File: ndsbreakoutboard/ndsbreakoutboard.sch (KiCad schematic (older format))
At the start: 2 parts, among them J1 Conn_01x17_Female, U1 ndsPADS

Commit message: Create footprint for the pad component (bottom of the cart). Basic PCB layout
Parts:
- J1: footprint (none) -> Connector_PinHeader_2.54mm:PinHeader_1x17_P2.54mm_Vertical
- U1: footprint (none) -> Connector:nds_contact_pads
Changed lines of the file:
@@
 F 0 "J1" V 2415 1980 50  0000 C CNN
 F 1 "Conn_01x17_Female" V 2324 1980 50  0000 C CNN
-F 2 "" H 2250 2000 50  0001 C CNN
+F 2 "Connector_PinHeader_2.54mm:PinHeader_1x17_P2.54mm_Vertical" H 2250 2000 50  0001 C CNN
 F 3 "~" H 2250 2000 50  0001 C CNN
 	1    2250 2000
@@
 F 0 "U1" H 2978 3942 50  0000 L CNN
 F 1 "ndsPADS" H 2978 3851 50  0000 L CNN
-F 2 "" H 2450 3400 50  0001 C CNN
+F 2 "Connector:nds_contact_pads" H 2450 3400 50  0001 C CNN
 F 3 "" H 2450 3400 50  0001 C CNN
 	1    2450 3400

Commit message: Commit before rebuilding netlist with pin headers
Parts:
- removed J1: Conn_01x17_Female, Connector_PinHeader_2.54mm:PinHeader_1x17_P2.54mm_Vertical, symbol Connector:Conn_01x17_Female
- added J1: Conn_01x01_Female, Connector_PinHeader_1.00mm:PinHeader_1x01_P1.00mm_Horizontal, symbol Connector:Conn_01x01_Female
- added J2: Conn_01x07_Female, Connector_PinHeader_1.00mm:PinHeader_1x07_P1.00mm_Horizontal, symbol Connector:Conn_01x07_Female
- added J3: Conn_01x08_Female, Connector_PinHeader_1.00mm:PinHeader_1x08_P1.00mm_Horizontal, symbol Connector:Conn_01x08_Female
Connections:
- net at U1.1 (GND): now also U1.17 (GND), J1.1 (Pin_1)
- net at U1.10 (D1): now also J3.7 (Pin_7)
- net at U1.11 (D2): now also J3.6 (Pin_6)
- net at U1.12 (D3): now also J3.5 (Pin_5)
- net at U1.13 (D5): now also J3.4 (Pin_4)
- net at U1.14 (D4): now also J3.3 (Pin_3)
- net at U1.15 (D6): now also J3.2 (Pin_2)
- net at U1.16 (D7): now also J3.1 (Pin_1)
- net at U1.2 (CLK): now also J2.7 (Pin_7)
- net at U1.3 (UNUSED): now also J2.6 (Pin_6)
- net at U1.4 (CS1_ROM): now also J2.5 (Pin_5)
- net at U1.5 (RESET): now also J2.4 (Pin_4)
- net at U1.6 (CS2_EEPROM): now also J2.3 (Pin_3)
- net at U1.7 (IRQ): now also J2.2 (Pin_2)
- net at U1.8 (3.3V): now also J2.1 (Pin_1)
- net at U1.9 (D0): now also J3.8 (Pin_8)
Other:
- moved on the sheet: U1
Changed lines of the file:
@@
 $EndDescr
-$Comp
-L Connector:Conn_01x17_Female J1
-U 1 1 5FF23434
-P 2250 2000
-F 0 "J1" V 2415 1980 50  0000 C CNN
-F 1 "Conn_01x17_Female" V 2324 1980 50  0000 C CNN
-F 2 "Connector_PinHeader_2.54mm:PinHeader_1x17_P2.54mm_Vertical" H 2250 2000 50  0001 C CNN
-F 3 "~" H 2250 2000 50  0001 C CNN
-	1    2250 2000
-	0    -1   -1   0
-$EndComp
 $Comp
 L Connector:ndsPADS U1
 U 1 1 5FF2F120
-P 2450 3400
-F 0 "U1" H 2978 3942 50  0000 L CNN
-F 1 "ndsPADS" H 2978 3851 50  0000 L CNN
-F 2 "Connector:nds_contact_pads" H 2450 3400 50  0001 C CNN
-F 3 "" H 2450 3400 50  0001 C CNN
-	1    2450 3400
+P 3050 2550
+F 0 "U1" H 3578 3092 50  0000 L CNN
+F 1 "ndsPADS" H 3578 3001 50  0000 L CNN
+F 2 "Connector:nds_contact_pads" H 3050 2550 50  0001 C CNN
+F 3 "" H 3050 2550 50  0001 C CNN
+	1    3050 2550
 	1    0    0    -1
 $EndComp
+$Comp
+L Connector:Conn_01x08_Female J3
+U 1 1 5FF67247
+P 3250 2450
+F 0 "J3" V 3323 2380 50  0000 C CNN
+F 1 "Conn_01x08_Female" V 3414 2380 50  0000 C CNN
+F 2 "Connector_PinHeader_1.00mm:PinHeader_1x08_P1.00mm_Horizontal" H 3250 2450 50  0001 C CNN
+F 3 "~" H 3250 2450 50  0001 C CNN
+	1    3250 2450
+	0    1    1    0
+$EndComp
+$Comp
+L Connector:Conn_01x07_Female J2
+U 1 1 5FF6AEC4
+P 2450 2450
+F 0 "J2" V 2523 2430 50  0000 C CNN
+F 1 "Conn_01x07_Female" V 2614 2430 50  0000 C CNN
+F 2 "Connector_PinHeader_1.00mm:PinHeader_1x07_P1.00mm_Horizontal" H 2450 2450 50  0001 C CNN
+F 3 "~" H 2450 2450 50  0001 C CNN
+	1    2450 2450
+	0    1    1    0
+$EndComp
+$Comp
+L Connector:Conn_01x01_Female J1
+U 1 1 5FF6C91E
+P 2050 3150
+F 0 "J1" V 1896 3198 50  0000 L CNN
+F 1 "Conn_01x01_Female" V 1987 3198 50  0000 L CNN
+F 2 "Connector_PinHeader_1.00mm:PinHeader_1x01_P1.00mm_Horizontal" H 2050 3150 50  0001 C CNN
+F 3 "~" H 2050 3150 50  0001 C CNN
+	1    2050 3150
+	0    1    1    0
+$EndComp
 Wire Wire Line
-	1450 2200 1450 3100
+	2050 2950 3650 2950
 Wire Wire Line
-	1550 2200 1550 3100
+	3650 2950 3650 2250
 Wire Wire Line
-	1650 2200 1650 3100
-Wire Wire Line
-	1750 2200 1750 3100
-Wire Wire Line
-	1850 2200 1850 3100
-Wire Wire Line
-	1950 2200 1950 3100
-Wire Wire Line
-	2050 2200 2050 3100
-Wire Wire Line
-	2150 2200 2150 3100
-Wire Wire Line
-	2250 2200 2250 3100
-Wire Wire Line
-	2350 2200 2350 3100
-Wire Wire Line
-	2450 2200 2450 3100
-Wire Wire Line
-	2550 2200 2550 3100
-Wire Wire Line
-	2650 2200 2650 3100
-Wire Wire Line
-	2750 3100 2750 2200
-Wire Wire Line
-	2850 2200 2850 3100
-Wire Wire Line
-	2950 2200 2950 3100
-Wire Wire Line
-	3050 2200 3050 3100
+	2050 2950 2050 2250
+Connection ~ 2050 2950
 $EndSCHEMATC

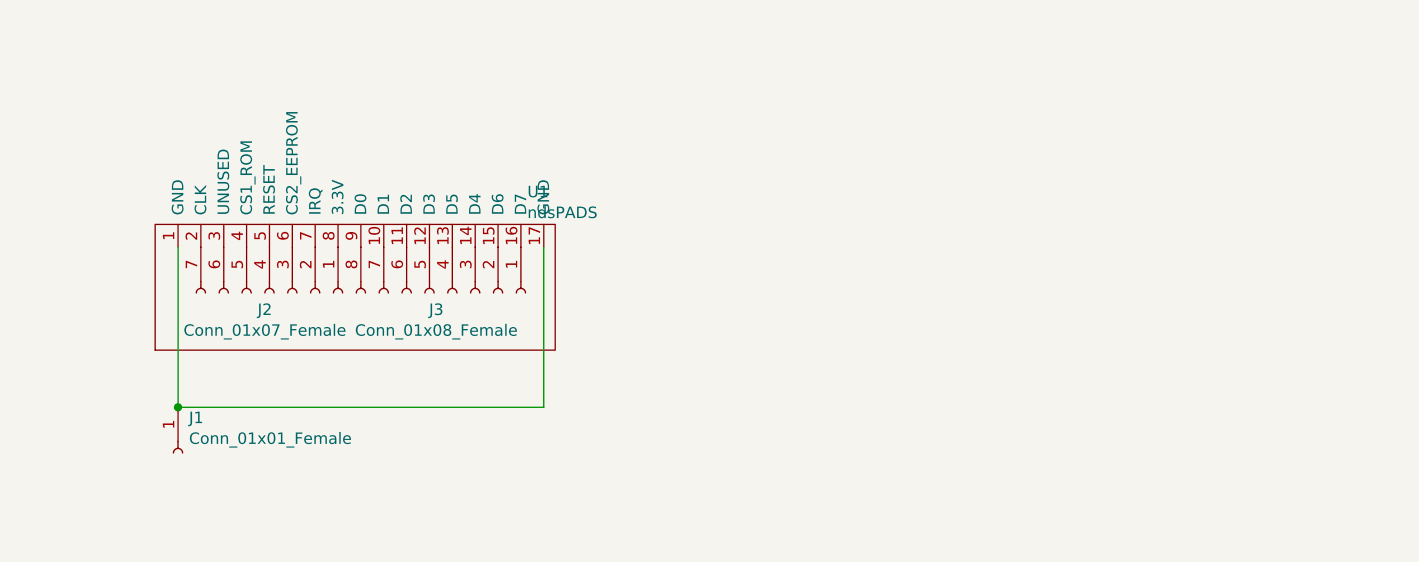
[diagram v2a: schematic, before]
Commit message: Final iteration finished
- correct eschematics
- pcb design finished
- pcb improvements
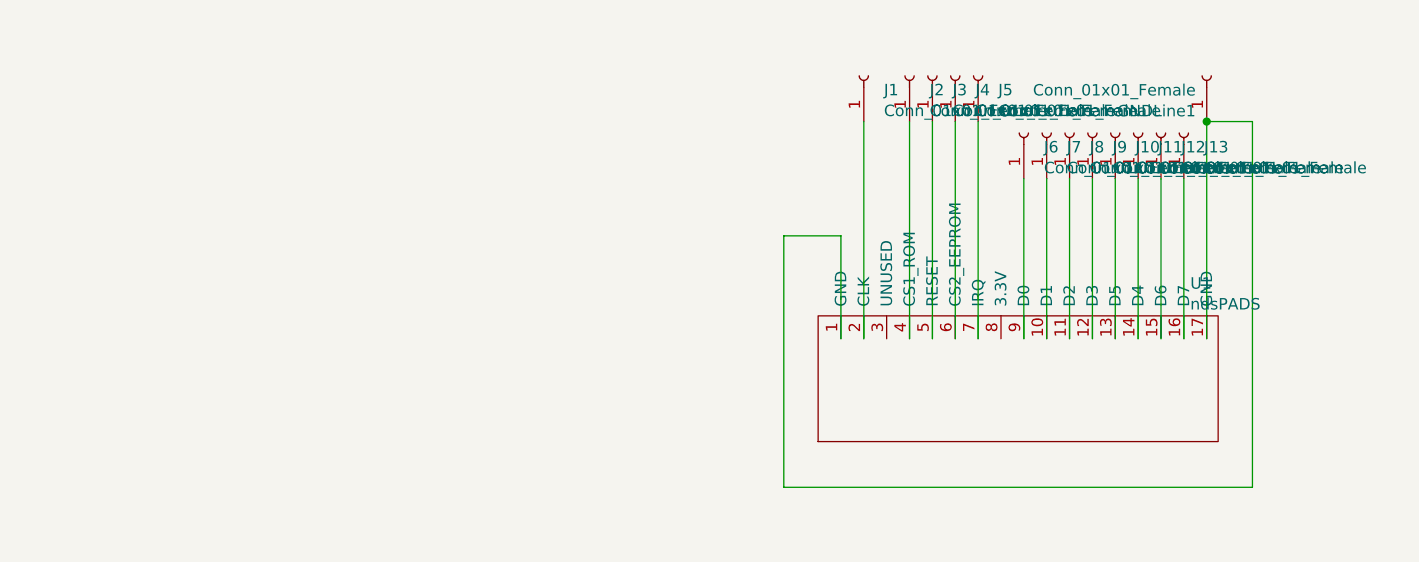
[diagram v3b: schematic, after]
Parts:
- removed J2: Conn_01x07_Female, Connector_PinHeader_1.00mm:PinHeader_1x07_P1.00mm_Horizontal, symbol Connector:Conn_01x07_Female
- removed J3: Conn_01x08_Female, Connector_PinHeader_1.00mm:PinHeader_1x08_P1.00mm_Horizontal, symbol Connector:Conn_01x08_Female
- added J1, J10, J11, J12, J13, J2, J3, J4, J5, J6, J7, J8, J9: Conn_01x01_Female, Connector_PinHeader_1.00mm:PinHeader_1x01_P1.00mm_Horizontal, symbol Connector:Conn_01x01_Female
- renumbered J1 to GNDLine1
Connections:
- net at U1.10 (D1): now also J7.1 (Pin_1)
- net at U1.11 (D2): now also J8.1 (Pin_1)
- net at U1.12 (D3): now also J9.1 (Pin_1)
- net at U1.13 (D5): now also J10.1 (Pin_1)
- net at U1.14 (D4): now also J11.1 (Pin_1)
- net at U1.15 (D6): now also J12.1 (Pin_1)
- net at U1.16 (D7): now also J13.1 (Pin_1)
- net at U1.2 (CLK): now also J1.1 (Pin_1)
- net at U1.4 (CS1_ROM): now also J2.1 (Pin_1)
- net at U1.5 (RESET): now also J3.1 (Pin_1)
- net at U1.6 (CS2_EEPROM): now also J4.1 (Pin_1)
- net at U1.7 (IRQ): now also J5.1 (Pin_1)
- net at U1.9 (D0): now also J6.1 (Pin_1)
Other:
- moved on the sheet: GNDLine1, U1
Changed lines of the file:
@@
 $EndDescr
+$Comp
+L Connector:Conn_01x01_Female GNDLine1
+U 1 1 5FF6C91E
+P 6550 1500
+F 0 "GNDLine1" V 6396 1548 50  0000 L CNN
+F 1 "Conn_01x01_Female" V 6487 1548 50  0000 L CNN
+F 2 "Connector_PinHeader_1.00mm:PinHeader_1x01_P1.00mm_Horizontal" H 6550 1500 50  0001 C CNN
+F 3 "~" H 6550 1500 50  0001 C CNN
+	1    6550 1500
+	0    -1   -1   0
+$EndComp
 $Comp
 L Connector:ndsPADS U1
 U 1 1 5FF2F120
-P 3050 2550
-F 0 "U1" H 3578 3092 50  0000 L CNN
-F 1 "ndsPADS" H 3578 3001 50  0000 L CNN
-F 2 "Connector:nds_contact_pads" H 3050 2550 50  0001 C CNN
-F 3 "" H 3050 2550 50  0001 C CNN
-	1    3050 2550
+P 5950 2950
+F 0 "U1" H 6478 3492 50  0000 L CNN
+F 1 "ndsPADS" H 6478 3401 50  0000 L CNN
+F 2 "Connector:nds_contact_pads" H 5950 2950 50  0001 C CNN
+F 3 "" H 5950 2950 50  0001 C CNN
+	1    5950 2950
 	1    0    0    -1
 $EndComp
-$Comp
-L Connector:Conn_01x08_Female J3
-U 1 1 5FF67247
-P 3250 2450
-F 0 "J3" V 3323 2380 50  0000 C CNN
-F 1 "Conn_01x08_Female" V 3414 2380 50  0000 C CNN
-F 2 "Connector_PinHeader_1.00mm:PinHeader_1x08_P1.00mm_Horizontal" H 3250 2450 50  0001 C CNN
-F 3 "~" H 3250 2450 50  0001 C CNN
-	1    3250 2450
-	0    1    1    0
-$EndComp
-$Comp
-L Connector:Conn_01x07_Female J2
-U 1 1 5FF6AEC4
-P 2450 2450
-F 0 "J2" V 2523 2430 50  0000 C CNN
-F 1 "Conn_01x07_Female" V 2614 2430 50  0000 C CNN
-F 2 "Connector_PinHeader_1.00mm:PinHeader_1x07_P1.00mm_Horizontal" H 2450 2450 50  0001 C CNN
-F 3 "~" H 2450 2450 50  0001 C CNN
-	1    2450 2450
-	0    1    1    0
+Wire Wire Line
+	6550 1700 6550 2650
+$Comp
+L Connector:Conn_01x01_Female J13
+U 1 1 5FFA52E0
+P 6450 1750
+F 0 "J13" V 6388 1662 50  0000 R CNN
+F 1 "Conn_01x01_Female" V 6297 1662 50  0000 R CNN
+F 2 "Connector_PinHeader_1.00mm:PinHeader_1x01_P1.00mm_Horizontal" H 6450 1750 50  0001 C CNN
+F 3 "~" H 6450 1750 50  0001 C CNN
+	1    6450 1750
+	0    -1   -1   0
+$EndComp
+$Comp
+L Connector:Conn_01x01_Female J12
+U 1 1 5FFA7926
+P 6350 1750
+F 0 "J12" V 6288 1662 50  0000 R CNN
+F 1 "Conn_01x01_Female" V 6197 1662 50  0000 R CNN
+F 2 "Connector_PinHeader_1.00mm:PinHeader_1x01_P1.00mm_Horizontal" H 6350 1750 50  0001 C CNN
+F 3 "~" H 6350 1750 50  0001 C CNN
+	1    6350 1750
+	0    -1   -1   0
+$EndComp
+$Comp
+L Connector:Conn_01x01_Female J11
+U 1 1 5FFA82DE
+P 6250 1750
+F 0 "J11" V 6188 1662 50  0000 R CNN
+F 1 "Conn_01x01_Female" V 6097 1662 50  0000 R CNN
+F 2 "Connector_PinHeader_1.00mm:PinHeader_1x01_P1.00mm_Horizontal" H 6250 1750 50  0001 C CNN
+F 3 "~" H 6250 1750 50  0001 C CNN
+	1    6250 1750
+	0    -1   -1   0
+$EndComp
+$Comp
+L Connector:Conn_01x01_Female J10
+U 1 1 5FFA8B42
+P 6150 1750
+F 0 "J10" V 6088 1662 50  0000 R CNN
+F 1 "Conn_01x01_Female" V 5997 1662 50  0000 R CNN
+F 2 "Connector_PinHeader_1.00mm:PinHeader_1x01_P1.00mm_Horizontal" H 6150 1750 50  0001 C CNN
+F 3 "~" H 6150 1750 50  0001 C CNN
+	1    6150 1750
+	0    -1   -1   0
+$EndComp
+$Comp
+L Connector:Conn_01x01_Female J9
+U 1 1 5FFA9474
+P 6050 1750
+F 0 "J9" V 5988 1662 50  0000 R CNN
+F 1 "Conn_01x01_Female" V 5897 1662 50  0000 R CNN
+F 2 "Connector_PinHeader_1.00mm:PinHeader_1x01_P1.00mm_Horizontal" H 6050 1750 50  0001 C CNN
+F 3 "~" H 6050 1750 50  0001 C CNN
+	1    6050 1750
+	0    -1   -1   0
+$EndComp
+$Comp
+L Connector:Conn_01x01_Female J8
+U 1 1 5FFA9A1A
+P 5950 1750
+F 0 "J8" V 5888 1662 50  0000 R CNN
+F 1 "Conn_01x01_Female" V 5797 1662 50  0000 R CNN
+F 2 "Connector_PinHeader_1.00mm:PinHeader_1x01_P1.00mm_Horizontal" H 5950 1750 50  0001 C CNN
+F 3 "~" H 5950 1750 50  0001 C CNN
+	1    5950 1750
+	0    -1   -1   0
+$EndComp
+$Comp
+L Connector:Conn_01x01_Female J7
+U 1 1 5FFA9F88
+P 5850 1750
+F 0 "J7" V 5788 1662 50  0000 R CNN
+F 1 "Conn_01x01_Female" V 5697 1662 50  0000 R CNN
+F 2 "Connector_PinHeader_1.00mm:PinHeader_1x01_P1.00mm_Horizontal" H 5850 1750 50  0001 C CNN
+F 3 "~" H 5850 1750 50  0001 C CNN
+	1    5850 1750
+	0    -1   -1   0
+$EndComp
+$Comp
+L Connector:Conn_01x01_Female J6
+U 1 1 5FFAA68B
+P 5750 1750
+F 0 "J6" V 5688 1662 50  0000 R CNN
+F 1 "Conn_01x01_Female" V 5597 1662 50  0000 R CNN
+F 2 "Connector_PinHeader_1.00mm:PinHeader_1x01_P1.00mm_Horizontal" H 5750 1750 50  0001 C CNN
+F 3 "~" H 5750 1750 50  0001 C CNN
+	1    5750 1750
+	0    -1   -1   0
+$EndComp
+Wire Wire Line
+	6450 1950 6450 2650
+Wire Wire Line
+	6350 1950 6350 2650
+Wire Wire Line
+	6250 1950 6250 2650
+Wire Wire Line
+	6150 1950 6150 2650
+Wire Wire Line
+	6050 1950 6050 2650
+Wire Wire Line
+	5950 1950 5950 2650
+Wire Wire Line
+	5850 1950 5850 2650
+Wire Wire Line
+	5750 1950 5750 2650
+$Comp
+L Connector:Conn_01x01_Female J5
+U 1 1 5FFAE11C
+P 5550 1500
+F 0 "J5" V 5488 1412 50  0000 R CNN
+F 1 "Conn_01x01_Female" V 5397 1412 50  0000 R CNN
+F 2 "Connector_PinHeader_1.00mm:PinHeader_1x01_P1.00mm_Horizontal" H 5550 1500 50  0001 C CNN
+F 3 "~" H 5550 1500 50  0001 C CNN
+	1    5550 1500
+	0    -1   -1   0
+$EndComp
+$Comp
+L Connector:Conn_01x01_Female J4
+U 1 1 5FFAEB09
+P 5450 1500
+F 0 "J4" V 5388 1412 50  0000 R CNN
+F 1 "Conn_01x01_Female" V 5297 1412 50  0000 R CNN
+F 2 "Connector_PinHeader_1.00mm:PinHeader_1x01_P1.00mm_Horizontal" H 5450 1500 50  0001 C CNN
+F 3 "~" H 5450 1500 50  0001 C CNN
+	1    5450 1500
+	0    -1   -1   0
+$EndComp
+$Comp
+L Connector:Conn_01x01_Female J3
+U 1 1 5FFAF6E1
+P 5350 1500
+F 0 "J3" V 5288 1412 50  0000 R CNN
+F 1 "Conn_01x01_Female" V 5197 1412 50  0000 R CNN
+F 2 "Connector_PinHeader_1.00mm:PinHeader_1x01_P1.00mm_Horizontal" H 5350 1500 50  0001 C CNN
+F 3 "~" H 5350 1500 50  0001 C CNN
+	1    5350 1500
+	0    -1   -1   0
+$EndComp
+$Comp
+L Connector:Conn_01x01_Female J2
+U 1 1 5FFB00D7
+P 5250 1500
+F 0 "J2" V 5188 1412 50  0000 R CNN
+F 1 "Conn_01x01_Female" V 5097 1412 50  0000 R CNN
+F 2 "Connector_PinHeader_1.00mm:PinHeader_1x01_P1.00mm_Horizontal" H 5250 1500 50  0001 C CNN
+F 3 "~" H 5250 1500 50  0001 C CNN
+	1    5250 1500
+	0    -1   -1   0
 $EndComp
 $Comp
 L Connector:Conn_01x01_Female J1
-U 1 1 5FF6C91E
-P 2050 3150
-F 0 "J1" V 1896 3198 50  0000 L CNN
-F 1 "Conn_01x01_Female" V 1987 3198 50  0000 L CNN
-F 2 "Connector_PinHeader_1.00mm:PinHeader_1x01_P1.00mm_Horizontal" H 2050 3150 50  0001 C CNN
-F 3 "~" H 2050 3150 50  0001 C CNN
-	1    2050 3150
-	0    1    1    0
-$EndComp
-Wire Wire Line
-	2050 2950 3650 2950
-Wire Wire Line
-	3650 2950 3650 2250
-Wire Wire Line
-	2050 2950 2050 2250
-Connection ~ 2050 2950
+U 1 1 5FFB0E31
+P 5050 1500
+F 0 "J1" V 4988 1412 50  0000 R CNN
+F 1 "Conn_01x01_Female" V 4897 1412 50  0000 R CNN
+F 2 "Connector_PinHeader_1.00mm:PinHeader_1x01_P1.00mm_Horizontal" H 5050 1500 50  0001 C CNN
+F 3 "~" H 5050 1500 50  0001 C CNN
+	1    5050 1500
+	0    -1   -1   0
+$EndComp
+Wire Wire Line
+	5550 1700 5550 2650
+Wire Wire Line
+	5450 1700 5450 2650
+Wire Wire Line
+	5350 1700 5350 2650
+Wire Wire Line
+	5250 1700 5250 2650
+Wire Wire Line
+	5050 1700 5050 2650
+Wire Wire Line
+	6550 1700 6750 1700
+Wire Wire Line
+	6750 1700 6750 3300
+Wire Wire Line
+	6750 3300 4700 3300
+Wire Wire Line
+	4700 3300 4700 2200
+Wire Wire Line
+	4700 2200 4950 2200
+Wire Wire Line
+	4950 2200 4950 2650
+Connection ~ 6550 1700
 $EndSCHEMATC

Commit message: Minor fixes
Schematic modified again, adding the mising unused pins and reflected in PCB
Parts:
- added J14, J15: Conn_01x01_Female, Connector_PinHeader_1.00mm:PinHeader_1x01_P1.00mm_Horizontal, symbol Connector:Conn_01x01_Female
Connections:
- net at U1.3 (UNUSED): now also J14.1 (Pin_1)
- net at U1.8 (3.3V): now also J15.1 (Pin_1)
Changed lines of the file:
@@
 	4950 2200 4950 2650
 Connection ~ 6550 1700
+$Comp
+L Connector:Conn_01x01_Female J14
+U 1 1 5FFBA68A
+P 5150 1250
+F 0 "J14" V 5088 1162 50  0000 R CNN
+F 1 "Conn_01x01_Female" V 4997 1162 50  0000 R CNN
+F 2 "Connector_PinHeader_1.00mm:PinHeader_1x01_P1.00mm_Horizontal" H 5150 1250 50  0001 C CNN
+F 3 "~" H 5150 1250 50  0001 C CNN
+	1    5150 1250
+	0    -1   -1   0
+$EndComp
+Wire Wire Line
+	5150 1450 5150 2650
+$Comp
+L Connector:Conn_01x01_Female J15
+U 1 1 5FFBCD3D
+P 5650 2000
+F 0 "J15" V 5588 1912 50  0000 R CNN
+F 1 "Conn_01x01_Female" V 5497 1912 50  0000 R CNN
+F 2 "Connector_PinHeader_1.00mm:PinHeader_1x01_P1.00mm_Horizontal" H 5650 2000 50  0001 C CNN
+F 3 "~" H 5650 2000 50  0001 C CNN
+	1    5650 2000
+	0    -1   -1   0
+$EndComp
+Wire Wire Line
+	5650 2200 5650 2650
 $EndSCHEMATC
